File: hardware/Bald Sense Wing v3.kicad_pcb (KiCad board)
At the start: 4 copper layers, 50.8 x 22.9 mm, 53 parts, among them J1 feather long, J2 feather short, J3 1140084168, J4 STEMMA-QT, Q1 Q_PNP_BEC, Q2 Q_NPN_BEC, SW1 PTS810, U1 APDS-9960, U2 DS3231MZ, U3 SHT30-DIS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

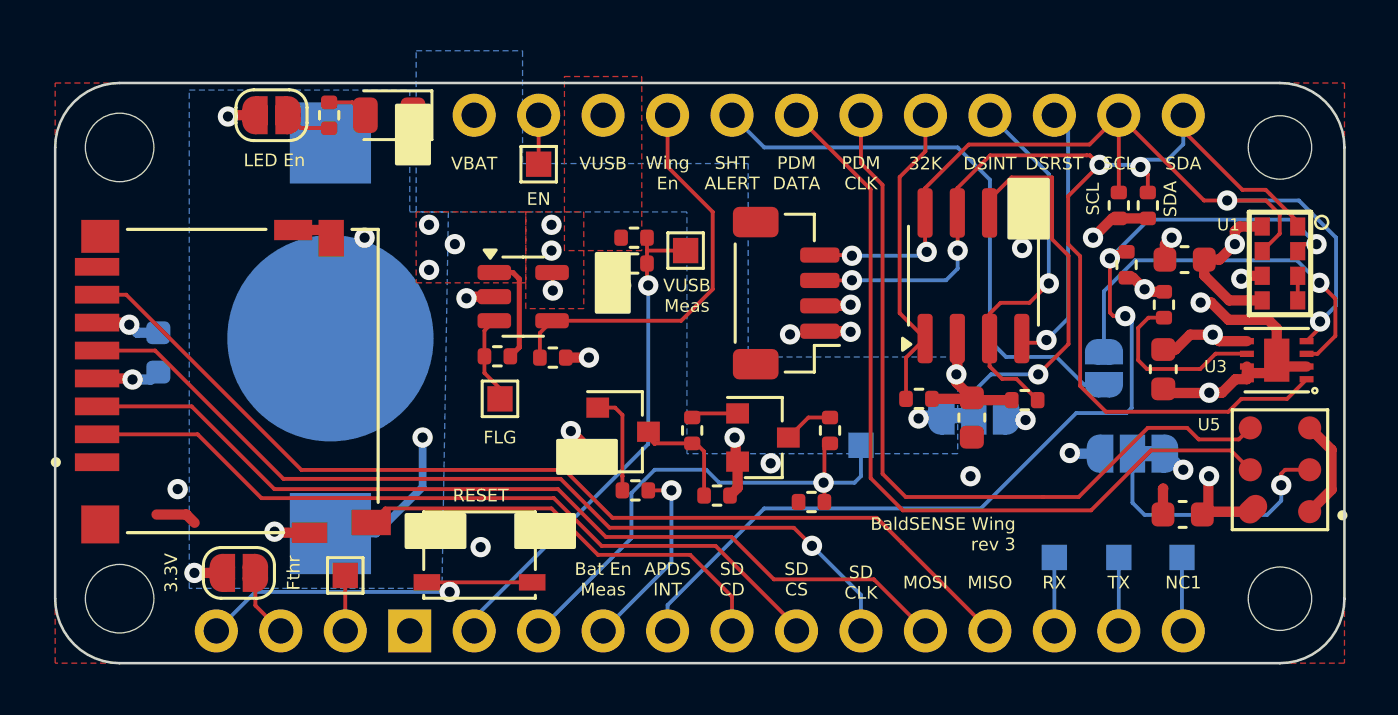
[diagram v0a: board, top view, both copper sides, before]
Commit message: design review changes incorporated
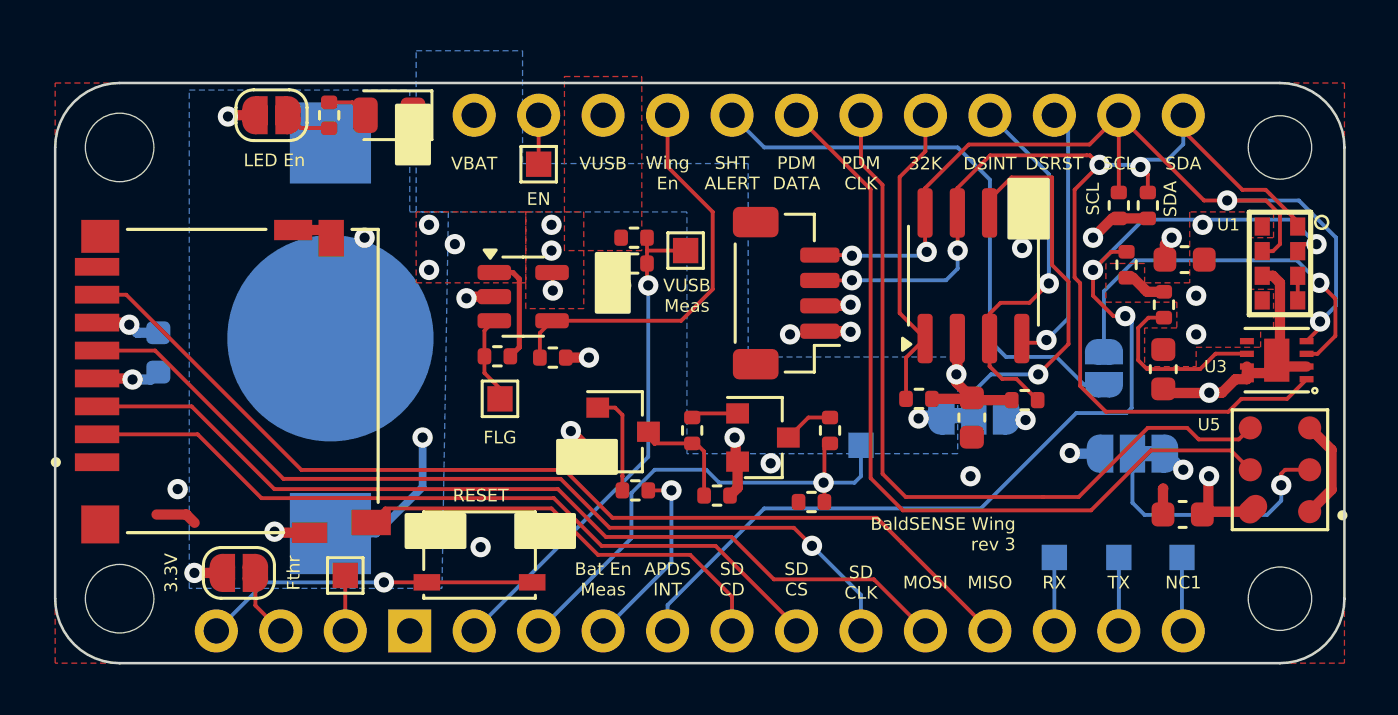
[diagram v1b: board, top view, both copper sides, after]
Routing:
- net +3.3V: track 35.1 -> 25.0 mm, vias 14 -> 13
- net /APDS_INT: track 39.8 -> 41.5 mm, vias 3 -> 4
- net GND: track 34.2 -> 32.6 mm, vias 20 -> 18
- net /~{RST}: track 14.0 -> 13.2 mm

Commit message: rev3 v2 fab submit
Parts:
- added TP10: Test Point, TestPoint:TestPoint_Pad_1.0x1.0mm, B.Cu at (53.3, 34.0)
- added TP11: Test Point, TestPoint:TestPoint_Pad_1.0x1.0mm, B.Cu at (62.2, 43.4)
- added TP12: Test Point, TestPoint:TestPoint_Pad_1.0x1.0mm, B.Cu at (59.7, 43.4)
- added TP13: Test Point, TestPoint:TestPoint_Pad_1.0x1.0mm, B.Cu at (56.1, 43.2)
- added TP14: Test Point, TestPoint:TestPoint_Pad_1.0x1.0mm, B.Cu at (53.3, 43.9)
- added TP15: Test Point, TestPoint:TestPoint_Pad_1.0x1.0mm, B.Cu at (42.9, 39.6)
- added TP16: Test Point, TestPoint:TestPoint_Pad_1.0x1.0mm, F.Cu at (36.8, 29.2)
- added TP17: Test Point, TestPoint:TestPoint_Pad_1.0x1.0mm, B.Cu at (59.7, 34.8)
- added TP18: Test Point, TestPoint:TestPoint_Pad_1.0x1.0mm, F.Cu at (66.0, 43.7)
- added TP9: Test Point, TestPoint:TestPoint_Pad_1.0x1.0mm, B.Cu at (53.3, 32.0)
- J4: value STEMMA-QT -> JST_SH_BM04B-SRSS-TB
- JP1: value 3.3V -> 3.3V Select
- SW1: value PTS810 -> PTS810SJK250SMTR LFS; footprint My Libraries:SW_SPST_PTS810_with_3D -> Button_Switch_SMD:SW_SPST_PTS810
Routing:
- net /SD_CD: track 17.2 -> 21.6 mm, vias 0 -> 1
- net /SD_CS: track 30.9 -> 34.4 mm
- net /SD_DOut: track 40.7 -> 44.2 mm
- net /SD_DIn: track 36.3 -> 39.9 mm
- net /SCL: track 38.1 -> 41.6 mm
- net /SDA: track 47.1 -> 50.6 mm
- net GND: track 32.6 -> 33.8 mm, vias 18 -> 19
- net /SD_CLK: track 35.5 -> 36.6 mm
- net /APDS_INT: vias 4 -> 3
